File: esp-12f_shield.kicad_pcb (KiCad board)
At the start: 2 copper layers, 48 x 53 mm, 56 parts, among them J1 UART, J10 Conn_01x01, J11 Conn_01x01, J12 Conn_01x01, J13 Conn_01x01, J2 SPI, J3 Sold_Pad_small, J5 Conn_01x01, J6 Conn_01x01, J7 Conn_01x01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

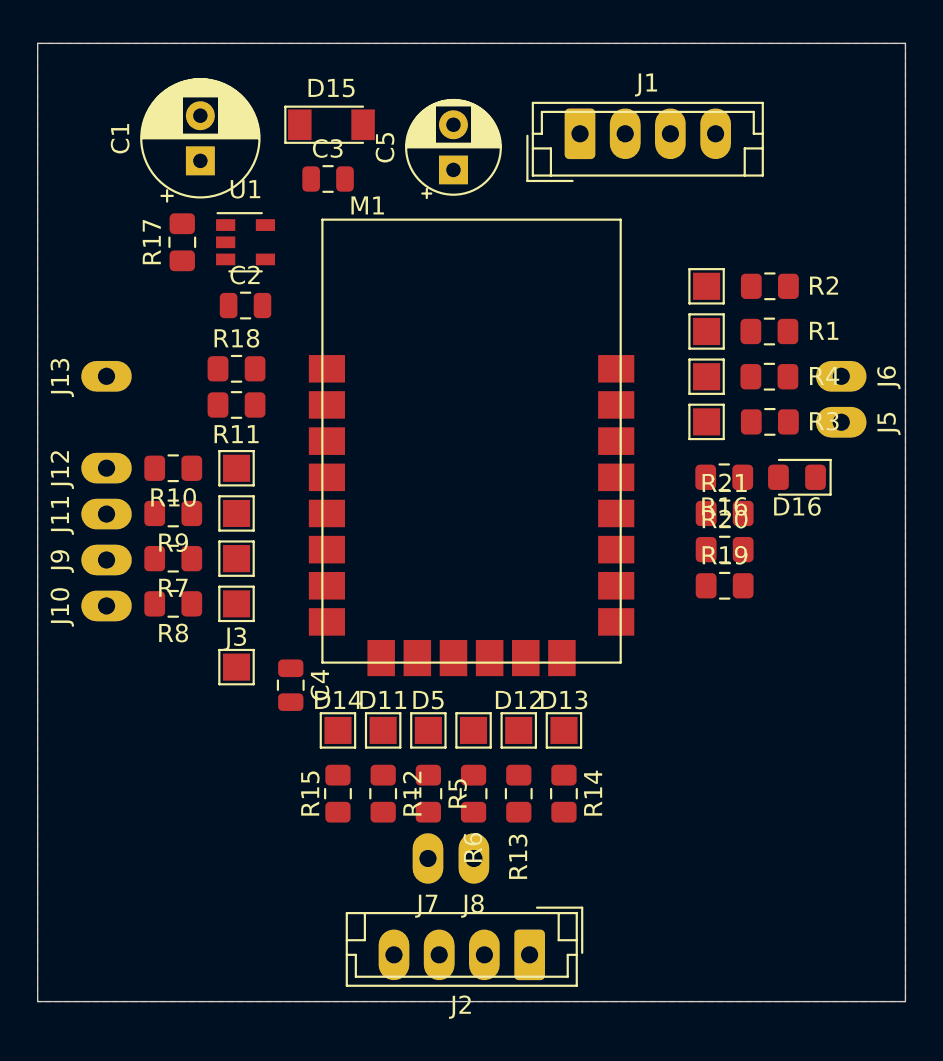
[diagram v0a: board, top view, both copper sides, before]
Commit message: paruosta schema ir plokste
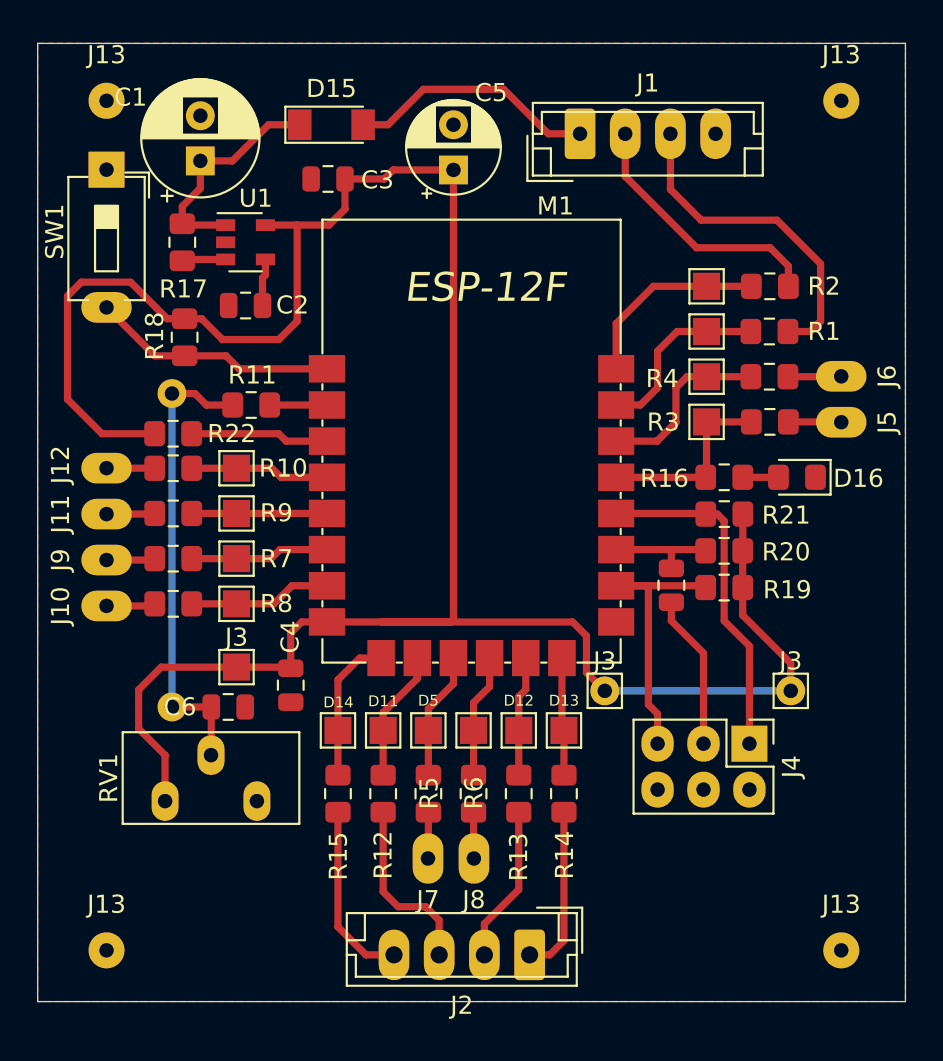
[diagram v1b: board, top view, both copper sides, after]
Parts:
- removed the J13 at (125.8, 88.4)
- added C6: 0.1, Capacitor_SMD:C_0805_2012Metric, F.Cu at (132.5, 106.7)
- added J13: Conn_01x01, Connector_Wire:SolderWirePad_1x01_Drill0.8mm, F.Cu at (166.4, 120.2)
- added J13: Conn_01x01, Connector_Wire:SolderWirePad_1x01_Drill0.8mm, F.Cu at (125.8, 120.2)
- added J13: Conn_01x01, Connector_Wire:SolderWirePad_1x01_Drill0.8mm, F.Cu at (125.8, 73.2)
- added J13: Conn_01x01, Connector_Wire:SolderWirePad_1x01_Drill0.8mm, F.Cu at (166.4, 73.2)
- added J3: Sold_Pad_small, TestPoint:TestPoint_Pad_1.5x1.5mm, F.Cu at (163.7, 105.8)
- added J3: Sold_Pad_small, TestPoint:TestPoint_Pad_1.5x1.5mm, F.Cu at (153.4, 105.8)
- added J4: Conn_02x03_Odd_Even, Connector_PinHeader_2.54mm:PinHeader_2x03_P2.54mm_Vertical, F.Cu at (161.4, 108.7)
- added R22: 10k, Resistor_SMD:R_0805_2012Metric_Pad1.15x1.40mm_HandSolder, F.Cu at (129.5, 91.6)
- added REF**: SolderWirePad_1x01_Drill0.8mm, Connector_Wire:SolderWirePad_1x01_Drill0.8mm, F.Cu at (129.4, 106.7)
- added REF**: SolderWirePad_1x01_Drill0.8mm, Connector_Wire:SolderWirePad_1x01_Drill0.8mm, F.Cu at (129.4, 89.4)
- added REF**: R_0805_2012Metric, Resistor_SMD:R_0805_2012Metric, F.Cu at (157.1, 100.0)
- added RV1: 10k, Potentiometer_THT:Potentiometer_Bourns_3296Y_Vertical, F.Cu at (129.0, 111.9)
- added SW1: Reset, Button_Switch_THT:SW_DIP_SPSTx01_Slide_6.7x4.1mm_W7.62mm_P2.54mm_LowProfile, F.Cu at (125.8, 77.0)
- moved R18 3.36 mm to (130.1, 86.3), turned to 270 degrees
- moved R11 0.81 mm to (133.8, 90.0), turned to 0 degrees
- moved R19 0.10 mm to (160.0, 100.1)
- moved R20 0.07 mm to (160.0, 98.1)
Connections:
- net /3V3 renamed +3V3
- J1 pad 2: /RXD -> /TXD
- J1 pad 3: /TXD -> /RXD
- M1 pad 2: /ADC -> Net-(M1-Pad2)
- M1 pad 3: /EN -> Net-(M1-Pad3)
- R11 pad 1: /ADC -> Net-(C6-Pad2)
- R11 pad 2: Net-(J13-Pad1) -> Net-(M1-Pad2)
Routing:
- net +3V3: track 0.00 -> 132.1 mm
- net Net-(C6-Pad2): track 0.00 -> 25.8 mm
- net Net-(J4-Pad1): track 0.00 -> 19.0 mm
- net /RXD: track 0.00 -> 18.3 mm
- net /IO15: track 0.00 -> 15.8 mm
- net Net-(J4-Pad3): track 0.00 -> 14.6 mm
- net /TXD: track 0.00 -> 14.6 mm
- net Net-(D15-Pad2): track 0.00 -> 13.8 mm
- net Net-(M1-Pad1): track 0.00 -> 13.6 mm
- net Net-(C1-Pad1): track 0.00 -> 12.6 mm
- net /TXD0: track 0.00 -> 10.8 mm
- net /IO4: track 0.00 -> 10.5 mm
- net /RXD0: track 0.00 -> 10.3 mm
- net Net-(J2-Pad4): track 0.00 -> 10.1 mm
- net Net-(J2-Pad3): track 0.00 -> 10.1 mm
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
